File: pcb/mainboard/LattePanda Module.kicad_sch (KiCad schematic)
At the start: 13 parts, among them J1 Conn_01x03_Pin

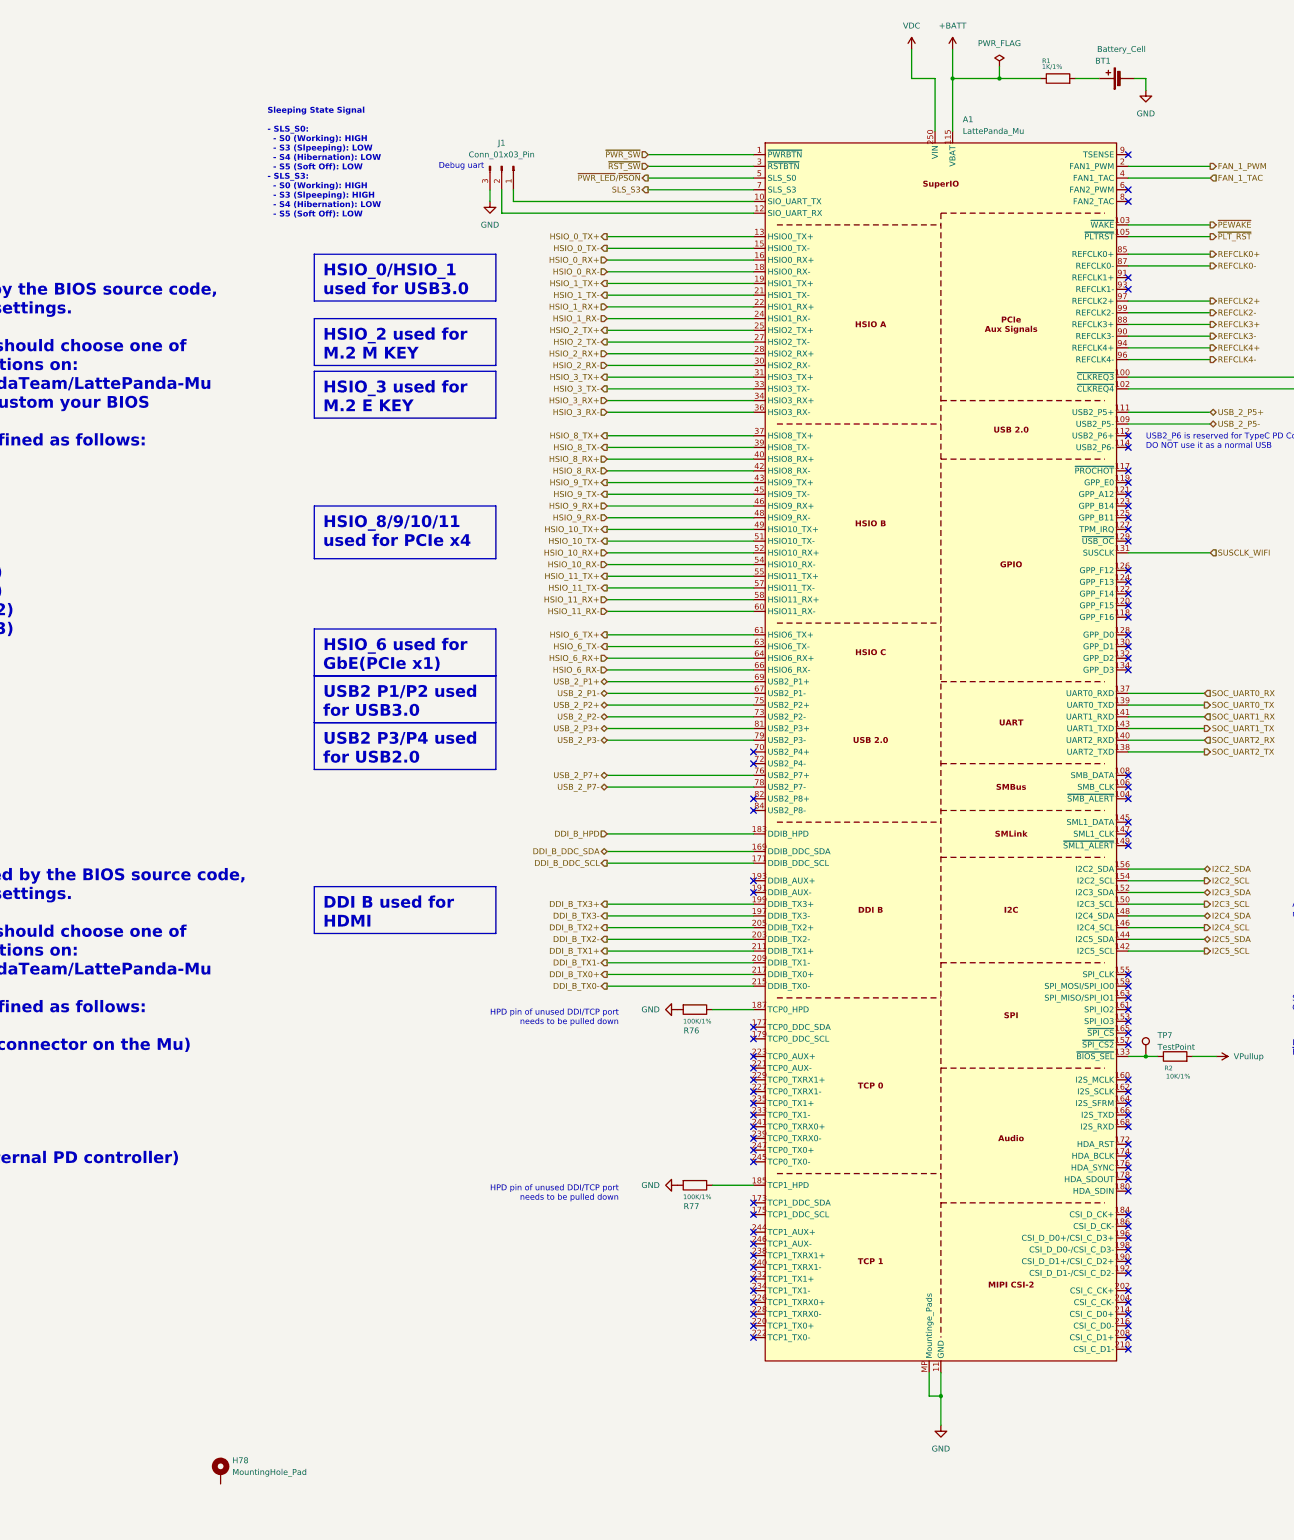
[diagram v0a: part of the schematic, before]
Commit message: a lot more routing has been done now
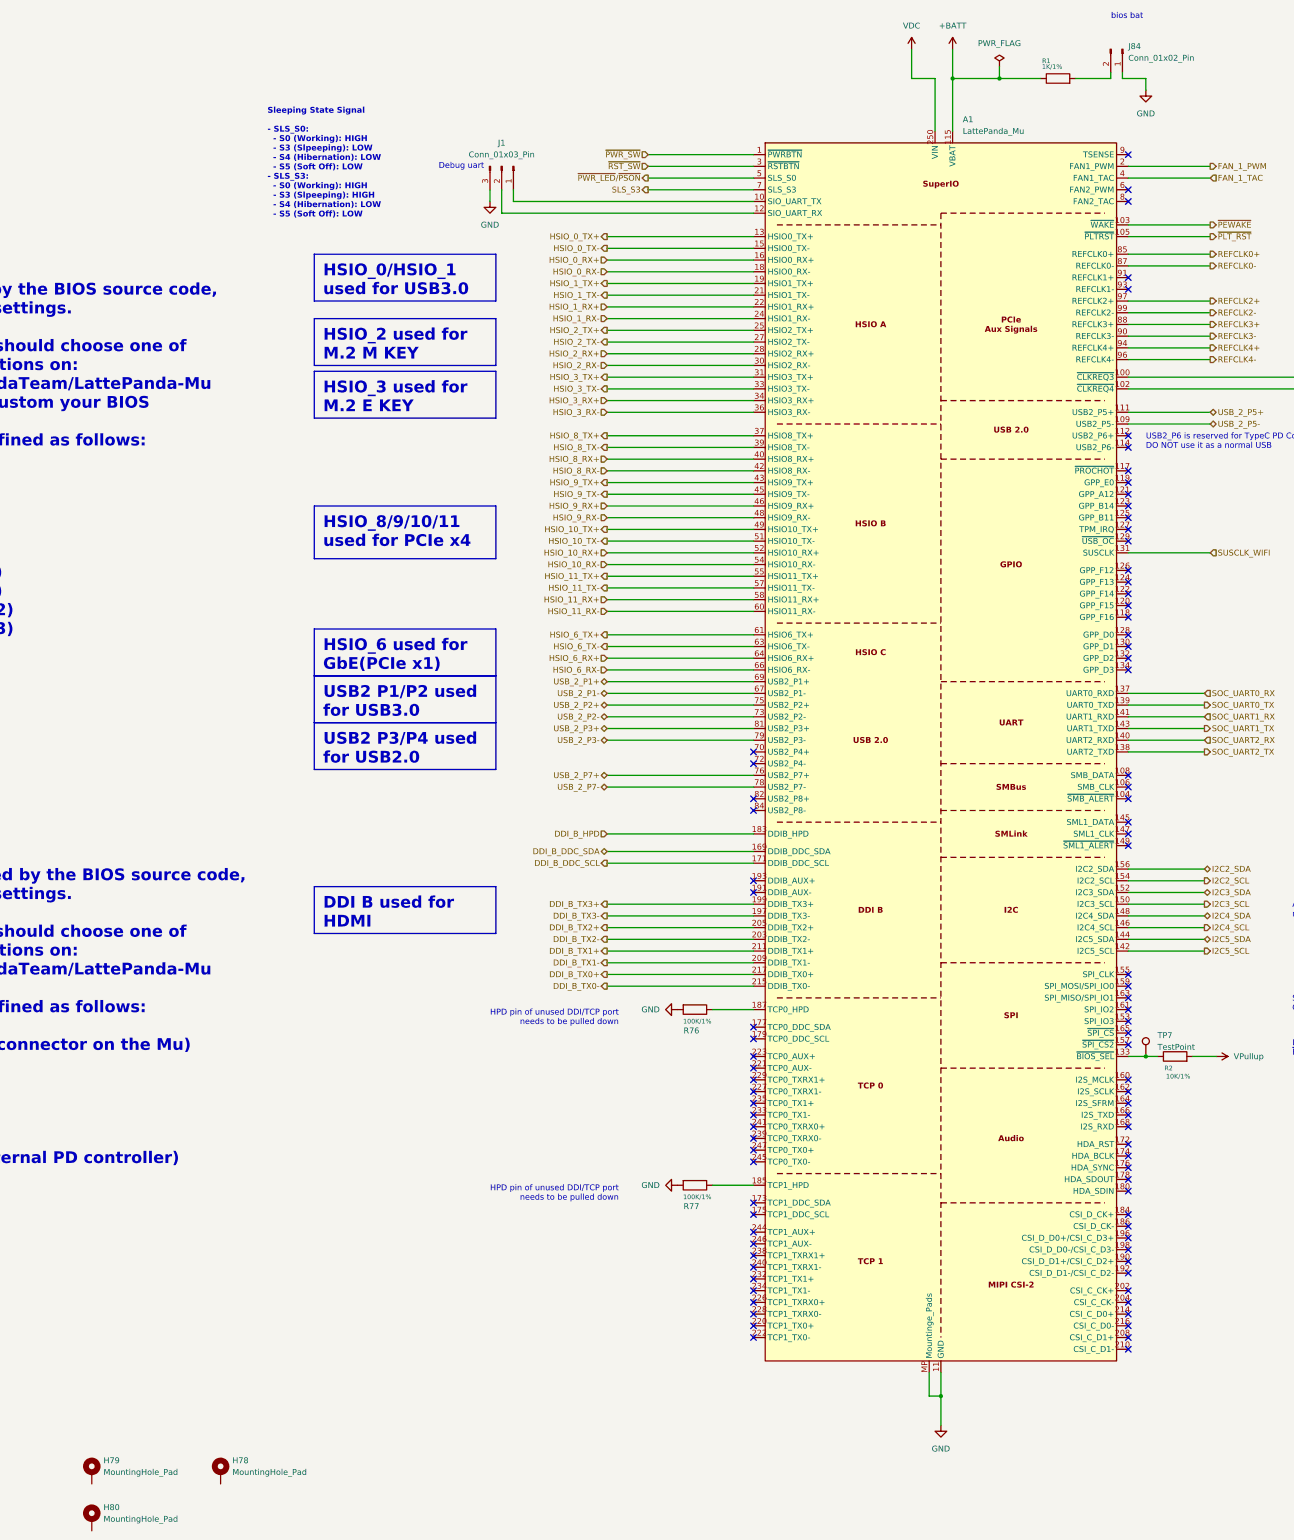
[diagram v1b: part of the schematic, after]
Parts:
- removed BT1: Battery_Cell, A_HDJ_Library:Battery_Holder_CR1220_S8411-45R, symbol Device:Battery_Cell
- added H79, H80: MountingHole_Pad, A_HDJ_Library:MountingHole_3mm_M2_Pad_TopOnly, symbol Mechanical:MountingHole_Pad
- added J84: Conn_01x02_Pin, Connector_PinHeader_2.54mm:PinHeader_1x02_P2.54mm_Vertical, symbol Connector:Conn_01x02_Pin
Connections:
- net GND: now also J84.1 (Pin_1)
- net at R1.2: now also J84.2 (Pin_2)
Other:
- note added: "bios bat"
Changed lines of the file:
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@@
 		)
 	)
+	(text "bios bat\n"
+		(exclude_from_sim no)
+		(at 351.536 30.988 0)
+		(effects
+			(font
+				(size 1.27 1.27)
+			)
+		)
+	)
 	(text "HPD pin of unused DDI/TCP port\nneeds to be pulled down"
 		(exclude_from_sim no)
@@
 	(wire
 		(pts
-			(xy 353.06 44.45) (xy 355.6 44.45)
+			(xy 351.79 233.68) (xy 368.3 233.68)
 		)
 		(stroke
@@
 	(wire
 		(pts
-			(xy 351.79 233.68) (xy 368.3 233.68)
+			(xy 304.8 44.45) (xy 309.88 44.45)
 		)
 		(stroke
@@
 	(wire
 		(pts
-			(xy 304.8 44.45) (xy 309.88 44.45)
+			(xy 350.52 44.45) (xy 355.6 44.45)
 		)
 		(stroke
@@
 	(wire
 		(pts
+			(xy 347.98 44.45) (xy 347.98 43.18)
+		)
+		(stroke
+			(width 0)
+			(type default)
+		)
+	)
+	(wire
+		(pts
 			(xy 351.79 180.34) (xy 368.3 180.34)
 		)
@@
 	(wire
 		(pts
-			(xy 340.36 44.45) (xy 345.44 44.45)
+			(xy 340.36 44.45) (xy 347.98 44.45)
 		)
 		(stroke
@@
 	(wire
 		(pts
+			(xy 350.52 43.18) (xy 350.52 44.45)
+		)
+		(stroke
+			(width 0)
+			(type default)
+		)
+	)
+	(wire
+		(pts
 			(xy 247.65 66.04) (xy 270.51 66.04)
 		)
@@
 	)
 	(symbol
+		(lib_name "MountingHole_Pad_1")
+		(lib_id "Mechanical:MountingHole_Pad")
+		(at 127 346.71 0)
+		(unit 1)
+		(exclude_from_sim no)
+		(in_bom no)
+		(on_board yes)
+		(dnp no)
+		(fields_autoplaced yes)
+		(property "Reference" "H79"
+			(at 129.54 344.1699 0)
+			(effects
+				(font
+					(size 1.27 1.27)
+				)
+				(justify left)
+			)
+		)
+		(property "Value" "MountingHole_Pad"
+			(at 129.54 346.7099 0)
+			(effects
+				(font
+					(size 1.27 1.27)
+				)
+				(justify left)
+			)
+		)
+		(property "Footprint" "A_HDJ_Library:MountingHole_3mm_M2_Pad_TopOnly"
+			(at 127 346.71 0)
+			(effects
+				(font
+					(size 1.27 1.27)
+				)
+				(hide yes)
+			)
+		)
+		(property "Datasheet" "~"
+			(at 127 346.71 0)
+			(effects
+				(font
+					(size 1.27 1.27)
+				)
+				(hide yes)
+			)
+		)
+		(property "Description" "Mounting Hole with connection"
+			(at 127 346.71 0)
+			(effects
+				(font
+					(size 1.27 1.27)
+				)
+				(hide yes)
+			)
+		)
+		(pin "1"
+		)
+		(instances
+			(project "[DFR1142]Lite Carrier for LattePanda Mu"
+				(path "/2a6d114a-7fd7-4207-b5f7-4ea9c34f36aa/6eee02c2-78c9-4e83-9ccf-e0f7690b57bf"
+					(reference "H79")
+					(unit 1)
+				)
+			)
+		)
+	)
+	(symbol
+		(lib_name "MountingHole_Pad_1")
+		(lib_id "Mechanical:MountingHole_Pad")
+		(at 127 356.87 0)
+		(unit 1)
+		(exclude_from_sim no)
+		(in_bom no)
+		(on_board yes)
+		(dnp no)
+		(fields_autoplaced yes)
+		(property "Reference" "H80"
+			(at 129.54 354.3299 0)
+			(effects
+				(font
+					(size 1.27 1.27)
+				)
+				(justify left)
+			)
+		)
+		(property "Value" "MountingHole_Pad"
+			(at 129.54 356.8699 0)
+			(effects
+				(font
+					(size 1.27 1.27)
+				)
+				(justify left)
+			)
+		)
+		(property "Footprint" "A_HDJ_Library:MountingHole_3mm_M2_Pad_TopOnly"
+			(at 127 356.87 0)
+			(effects
+				(font
+					(size 1.27 1.27)
+				)
+				(hide yes)
+			)
+		)
+		(property "Datasheet" "~"
+			(at 127 356.87 0)
+			(effects
+				(font
+					(size 1.27 1.27)
+				)
+				(hide yes)
+			)
+		)
+		(property "Description" "Mounting Hole with connection"
+			(at 127 356.87 0)
+			(effects
+				(font
+					(size 1.27 1.27)
+				)
+				(hide yes)
+			)
+		)
+		(pin "1"
+		)
+		(instances
+			(project "[DFR1142]Lite Carrier for LattePanda Mu"
+				(path "/2a6d114a-7fd7-4207-b5f7-4ea9c34f36aa/6eee02c2-78c9-4e83-9ccf-e0f7690b57bf"
+					(reference "H80")
+					(unit 1)
+				)
+			)
+		)
+	)
+	(symbol
 		(lib_id "power:GND")
 		(at 414.02 302.26 0)
@@
 	)
 	(symbol
-		(lib_id "Device:Battery_Cell")
-		(at 350.52 44.45 90)
+		(lib_id "Connector:Conn_01x02_Pin")
+		(at 350.52 38.1 270)
 		(unit 1)
 		(exclude_from_sim no)
@@
 		(on_board yes)
 		(dnp no)
-		(property "Reference" "BT1"
-			(at 347.98 40.64 90)
+		(fields_autoplaced yes)
+		(property "Reference" "J84"
+			(at 351.79 37.4649 90)
 			(effects
 				(font
@@
 			)
 		)
-		(property "Value" "Battery_Cell"
-			(at 355.6 38.1 90)
+		(property "Value" "Conn_01x02_Pin"
+			(at 351.79 40.0049 90)
 			(effects
 				(font
@@
 			)
 		)
-		(property "Footprint" "A_HDJ_Library:Battery_Holder_CR1220_S8411-45R"
-			(at 348.996 44.45 90)
+		(property "Footprint" "Connector_PinHeader_2.54mm:PinHeader_1x02_P2.54mm_Vertical"
+			(at 350.52 38.1 0)
 			(effects
 				(font
@@
 		)
 		(property "Datasheet" "~"
-			(at 348.996 44.45 90)
+			(at 350.52 38.1 0)
 			(effects
 				(font
@@
 			)
 		)
-		(property "Description" ""
-			(at 350.52 44.45 0)
+		(property "Description" "Generic connector, single row, 01x02, script generated"
+			(at 350.52 38.1 0)
 			(effects
 				(font
@@
 			)
 		)
-		(property "SCH_Show_Footprint" ""
-			(at 350.52 44.45 0)
-			(effects
-				(font
-					(size 1.27 1.27)
-				)
-				(hide yes)
-			)
-		)
-		(property "Sim.Device" ""
-			(at 350.52 44.45 0)
-			(effects
-				(font
-					(size 1.27 1.27)
-				)
-				(hide yes)
-			)
-		)
-		(property "Sim.Pins" ""
-			(at 350.52 44.45 0)
-			(effects
-				(font
-					(size 1.27 1.27)
-				)
-				(hide yes)
-			)
-		)
-		(property "Sim.Type" ""
-			(at 350.52 44.45 0)
-			(effects
-				(font
-					(size 1.27 1.27)
-				)
-				(hide yes)
-			)
+		(pin "2"
 		)
 		(pin "1"
 		)
-		(pin "2"
-		)
 		(instances
-			(project "[DFR1142]Lite Carrier for LattePanda Mu"
+			(project ""
 				(path "/2a6d114a-7fd7-4207-b5f7-4ea9c34f36aa/6eee02c2-78c9-4e83-9ccf-e0f7690b57bf"
-					(reference "BT1")
+					(reference "J84")
 					(unit 1)
 				)

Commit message: before i aply ungrounding changes to moutning holes
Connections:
- net GND: no longer H5.1, H6.1
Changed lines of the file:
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@@
-	)
-	(symbol
-		(lib_id "power:GND")
-		(at 439.42 302.26 0)
-		(unit 1)
-		(exclude_from_sim no)
-		(in_bom yes)
-		(on_board yes)
-		(dnp no)
-		(fields_autoplaced yes)
-		(property "Reference" "#PWR012"
-			(at 439.42 308.61 0)
-			(effects
-				(font
-					(size 1.27 1.27)
-				)
-				(hide yes)
-			)
-		)
-		(property "Value" "GND"
-			(at 439.42 307.34 0)
-			(effects
-				(font
-					(size 1.27 1.27)
-				)
-			)
-		)
-		(property "Footprint" ""
-			(at 439.42 302.26 0)
-			(effects
-				(font
-					(size 1.27 1.27)
-				)
-				(hide yes)
-			)
-		)
-		(property "Datasheet" ""
-			(at 439.42 302.26 0)
-			(effects
-				(font
-					(size 1.27 1.27)
-				)
-				(hide yes)
-			)
-		)
-		(property "Description" ""
-			(at 439.42 302.26 0)
-			(effects
-				(font
-					(size 1.27 1.27)
-				)
-				(hide yes)
-			)
-		)
-		(pin "1"
-		)
-		(instances
-			(project "[DFR1142]Lite Carrier for LattePanda Mu"
-				(path "/2a6d114a-7fd7-4207-b5f7-4ea9c34f36aa/6eee02c2-78c9-4e83-9ccf-e0f7690b57bf"
-					(reference "#PWR012")
-					(unit 1)
-				)
-			)
-		)
 	)
 	(symbol
@@
 					(unit 1)
 				)
-			)
-		)
-	)
-	(symbol
-		(lib_id "power:GND")
-		(at 414.02 302.26 0)
-		(unit 1)
-		(exclude_from_sim no)
-		(in_bom yes)
-		(on_board yes)
-		(dnp no)
-		(fields_autoplaced yes)
-		(property "Reference" "#PWR011"
-			(at 414.02 308.61 0)
-			(effects
-				(font
-					(size 1.27 1.27)
-				)
-				(hide yes)
-			)
-		)
-		(property "Value" "GND"
-			(at 414.02 307.34 0)
-			(effects
-				(font
-					(size 1.27 1.27)
-				)
-			)
-		)
-		(property "Footprint" ""
-			(at 414.02 302.26 0)
-			(effects
-				(font
-					(size 1.27 1.27)
-				)
-				(hide yes)
-			)
-		)
-		(property "Datasheet" ""
-			(at 414.02 302.26 0)
-			(effects
-				(font
-					(size 1.27 1.27)
-				)
-				(hide yes)
-			)
-		)
-		(property "Description" ""
-			(at 414.02 302.26 0)
-			(effects
-				(font
-					(size 1.27 1.27)
-				)
-				(hide yes)
-			)
-		)
-		(pin "1"
-		)
-		(instances
-			(project "[DFR1142]Lite Carrier for LattePanda Mu"
-				(path "/2a6d114a-7fd7-4207-b5f7-4ea9c34f36aa/6eee02c2-78c9-4e83-9ccf-e0f7690b57bf"
-					(reference "#PWR011")
-					(unit 1)
-				)

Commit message: a
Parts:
- H78, H79, H80: now in the parts list
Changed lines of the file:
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@@
 		(unit 1)
 		(exclude_from_sim no)
-		(in_bom no)
+		(in_bom yes)
 		(on_board yes)
 		(dnp no)
@@
 		(unit 1)
 		(exclude_from_sim no)
-		(in_bom no)
+		(in_bom yes)
 		(on_board yes)
 		(dnp no)
@@
 		(unit 1)
 		(exclude_from_sim no)
-		(in_bom no)
-		(on_board yes)
-		(dnp no)
+		(in_bom yes)
+		(on_board yes)
+		(dnp no)
